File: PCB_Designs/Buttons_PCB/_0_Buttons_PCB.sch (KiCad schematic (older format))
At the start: 83 parts, among them P1 CONN_01X05, P2 CONN_01X01, P3 CONN_01X01, P4 CONN_01X01, U1 CHERRY-MX, U10 CHERRY-MX, U11 CHERRY-MX, U12 CHERRY-MX, U13 MCP23017, U14 MCP23017, U2 CHERRY-MX, U3 CHERRY-MX, U4 CHERRY-MX, U5 CHERRY-MX, U6 CHERRY-MX, U7 CHERRY-MX, U8 CHERRY-MX, U9 CHERRY-MX

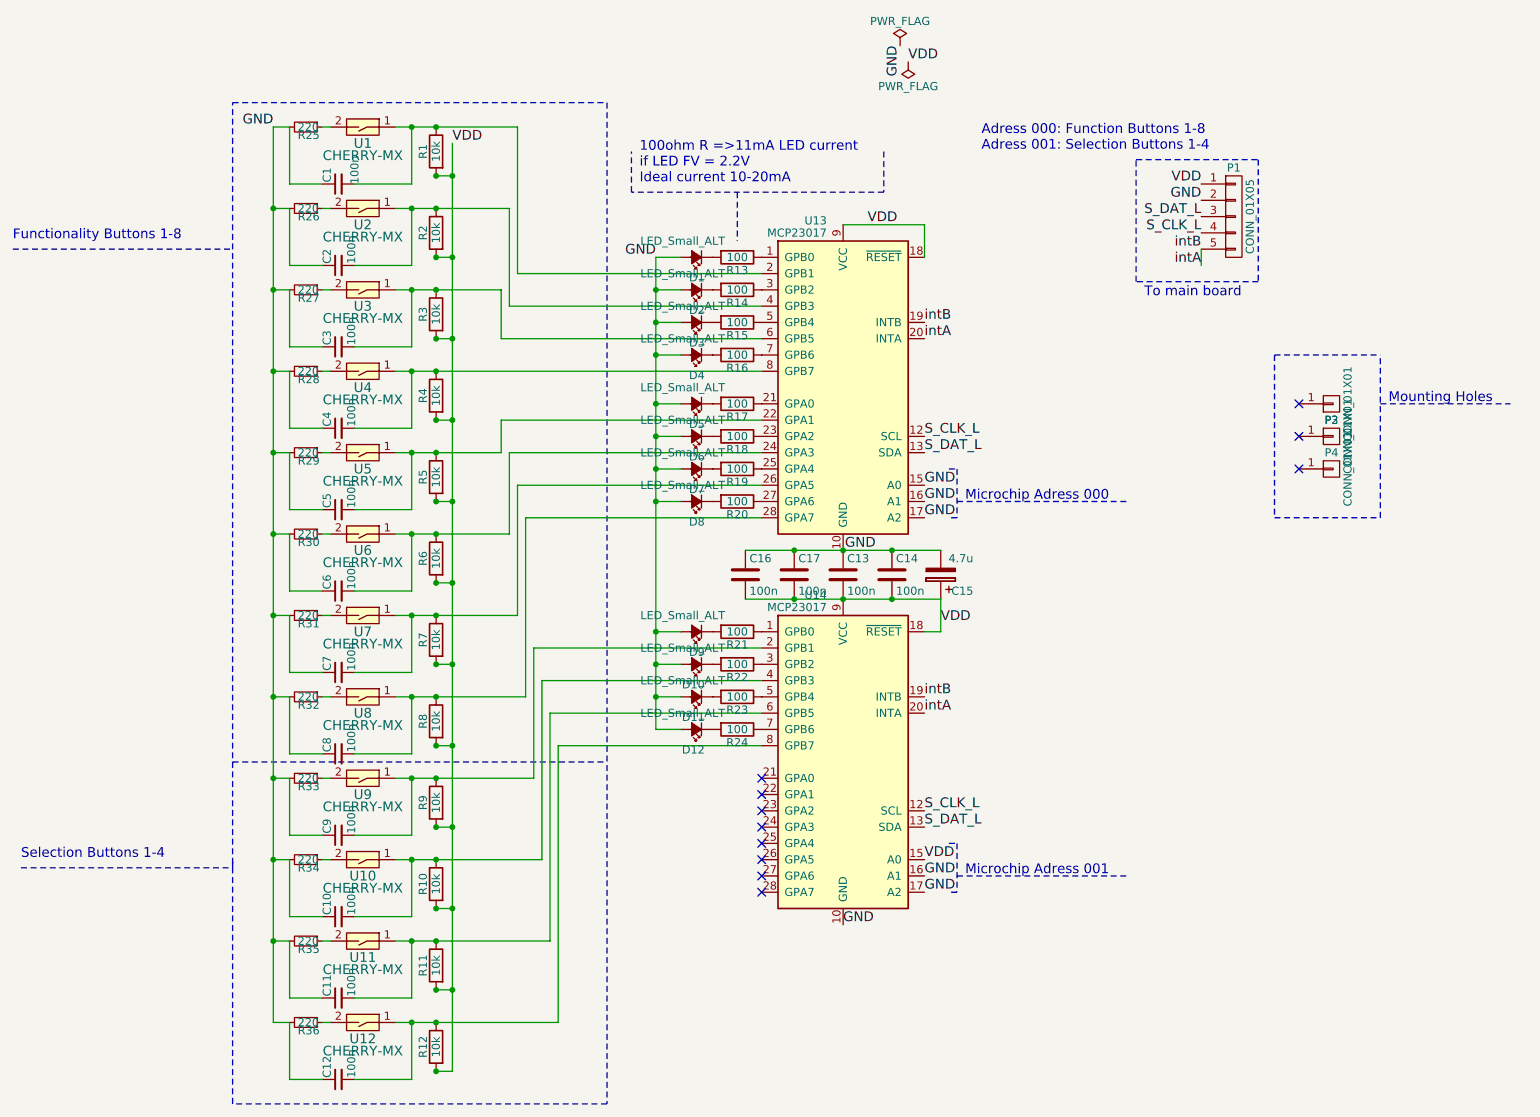
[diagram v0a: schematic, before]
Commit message: Buttons V4
Pulldown changed to pullup in button switch filter.
Filter to switch completed (changed).
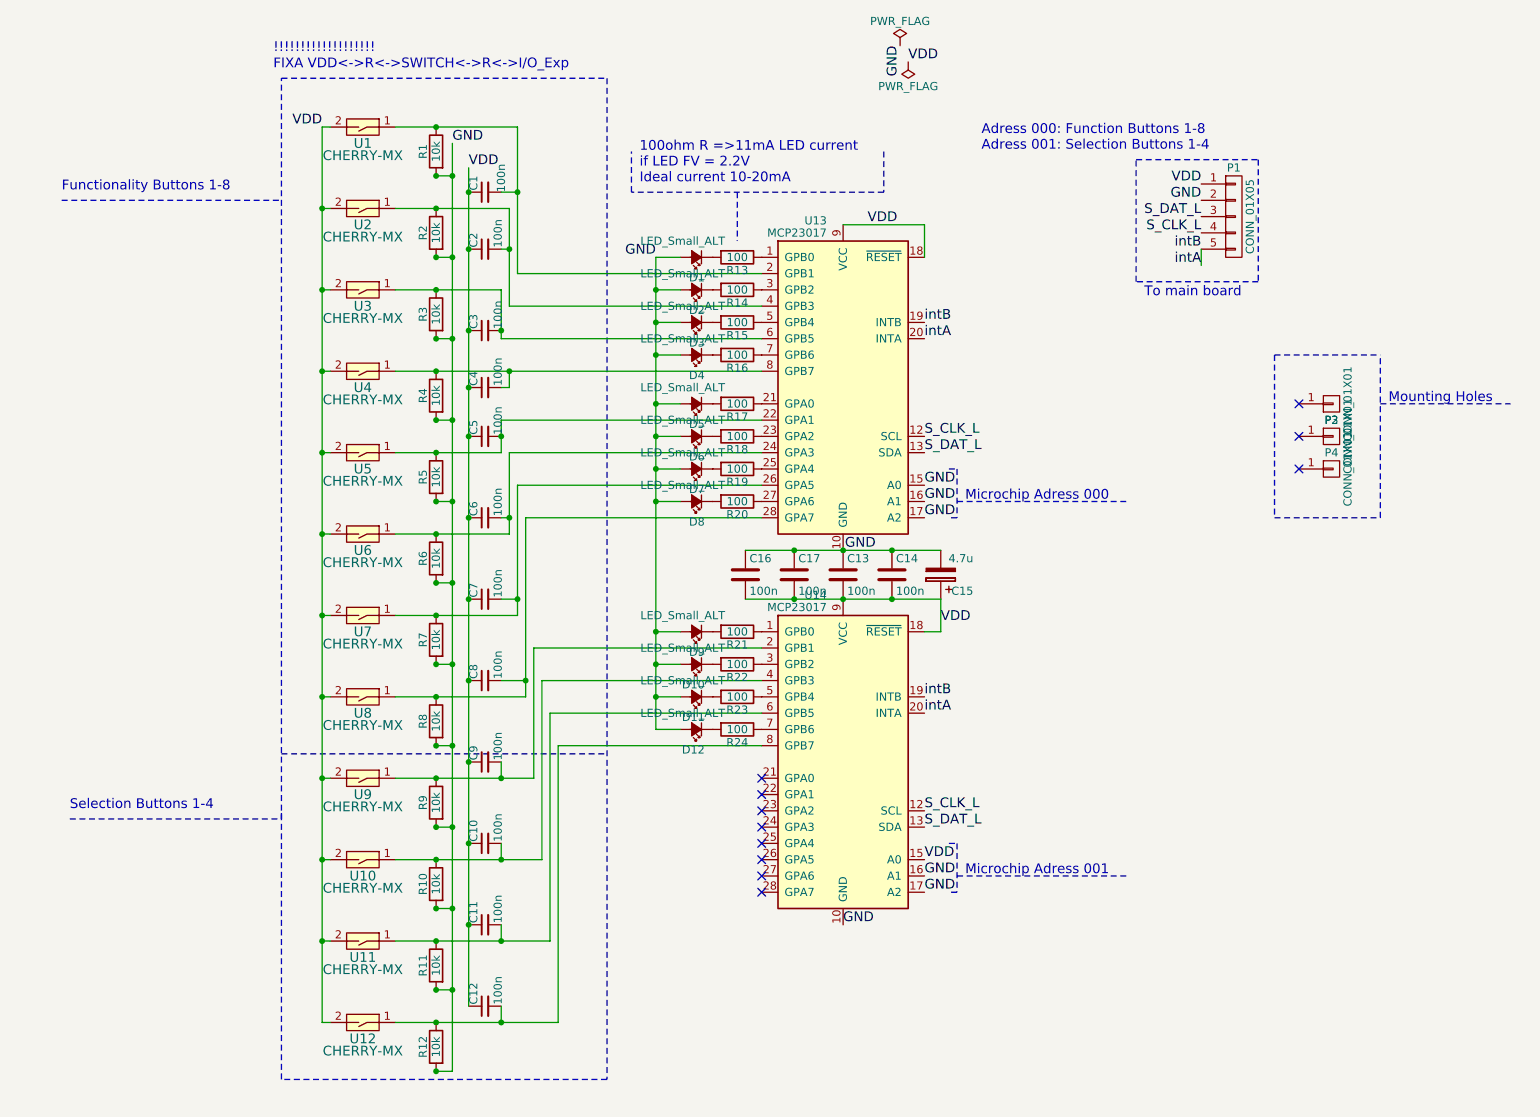
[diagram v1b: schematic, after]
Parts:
- removed R25, R26, R27, R28, R29, R30, R31, R32, R33, R34, R35, R36: 220, Resistors_SMD:R_0603_HandSoldering, symbol R_Small
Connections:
- net GND: now also R1.2, R10.2, R11.2, R12.2, R2.2, R3.2, R4.2, R5.2, R6.2, R7.2, R8.2, R9.2; no longer C1.1, C10.1, C11.1, C12.1, C2.1, C3.1, C4.1, C5.1, C6.1, C7.1, C8.1, C9.1
- net VDD: now also C1.1, C10.1, C11.1, C12.1, C2.1, C3.1, C4.1, C5.1, C6.1, C7.1, C8.1, C9.1, U1.2, U10.2, U11.2, U12.2, U2.2, U3.2, U4.2, U5.2, U6.2, U7.2, U8.2, U9.2; no longer R1.2, R10.2, R11.2, R12.2, R2.2, R3.2, R4.2, R5.2, R6.2, R7.2, R8.2, R9.2
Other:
- note added: "!!!!!!!!!!!!!!!!!!!"
- note added: "FIXA VDD<->R<->SWITCH<->R<->I/O_Exp"
- moved on the sheet: C1, C10, C11, C12, C2, C3, C4, C5, C6, C7, C8, C9
